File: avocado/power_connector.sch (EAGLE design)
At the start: 1 part

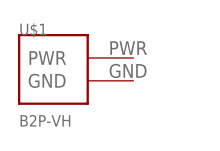
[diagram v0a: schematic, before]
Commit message: finalized optical encoder and power connector boards
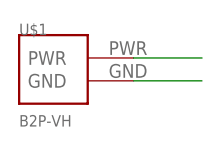
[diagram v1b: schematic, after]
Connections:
- new net GND: U$1.GND
- new net PWR: U$1.PWR
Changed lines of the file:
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@@
 </busses>
 <nets>
+<net name="PWR" class="0">
+<segment>
+<pinref part="U$1" gate="G$1" pin="PWR"/>
+<wire x1="7.62" y1="2.54" x2="15.24" y2="2.54" width="0.1524" layer="91"/>
+</segment>
+</net>
+<net name="GND" class="0">
+<segment>
+<pinref part="U$1" gate="G$1" pin="GND"/>
+<wire x1="7.62" y1="0" x2="15.24" y2="0" width="0.1524" layer="91"/>
+</segment>
+</net>
 </nets>
 </sheet>
